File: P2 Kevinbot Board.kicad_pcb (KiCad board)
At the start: 2 copper layers, 196.5 x 95.4 mm, 76 parts, among them J1 Screw_Terminal_01x02, J10 Conn_01x04, J11 Conn_01x04_Male, J12 Conn_02x06_Odd_Even, J13 Conn_01x04, J14 Conn_01x02, J15 Conn_01x04, J16 Conn_02x06_Odd_Even, J17 Conn_04x03_Servo, J18 Conn_04x03_Servo, J19 Conn_04x03_Servo, J2 Conn_01x03_Male, J20 Conn_04x03_Servo, J21 Conn_01x02, J22 Conn_01x05, J23 Conn_01x05, J24 Conn_01x05, J25 Conn_01x05, J26 Conn_04x03_Servo, J27 Conn_04x03_Servo, J28 Conn_04x03_Servo, J29 Conn_04x03_Servo, J3 Screw_Terminal_01x02, J30 Conn_01x02_Pin, J31 Conn_01x02, J4 Screw_Terminal_01x02, J5 Screw_Terminal_01x02, J6 Conn_02x06_Odd_Even, J7 Conn_01x04, J8 Conn_02x06_Odd_Even, J9 Screw_Terminal_01x02, Q1 IRLML6402, SW1 SW_Push, U1 P2_EDGE_MODULE_SOCKET, U2 DS18B20, U3 PCA9685PW, U4 TC4427, U5 PCA9685PW

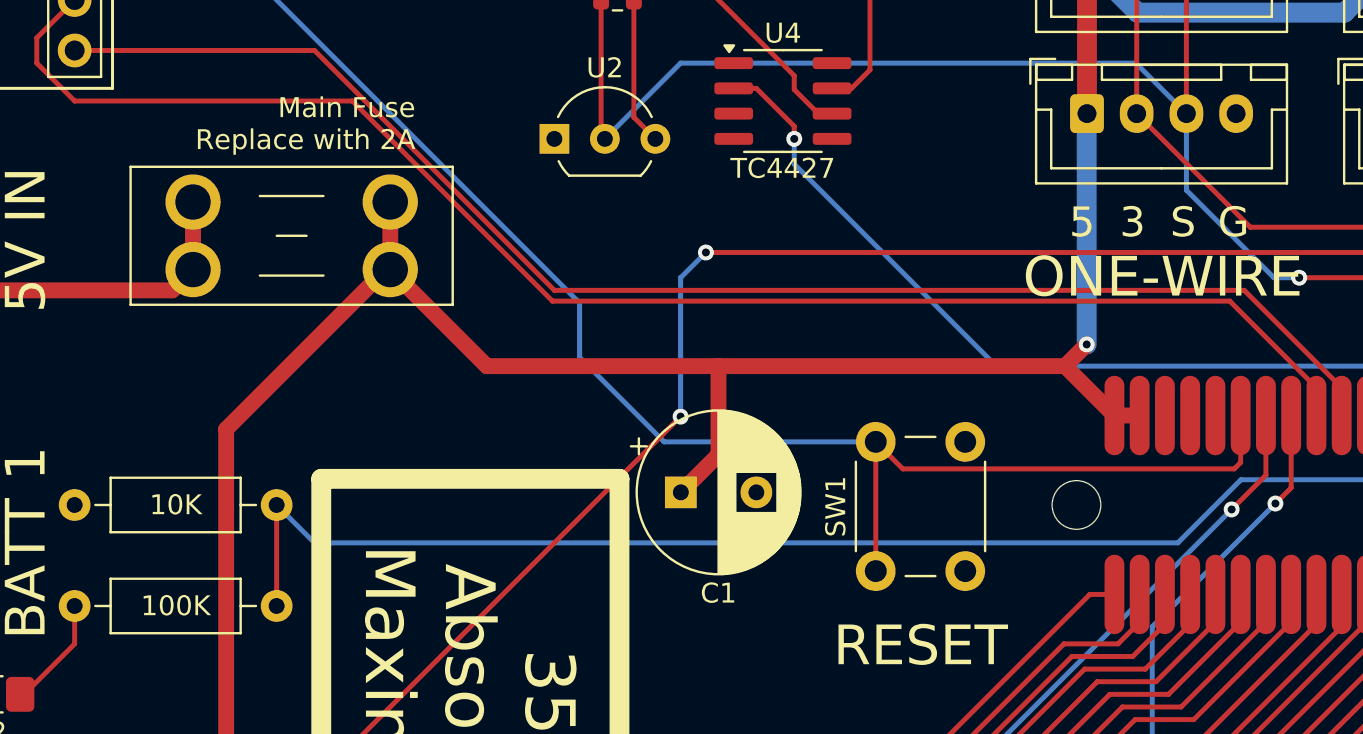
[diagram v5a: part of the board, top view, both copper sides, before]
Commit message: Add mfr part numbers and datasheets to all
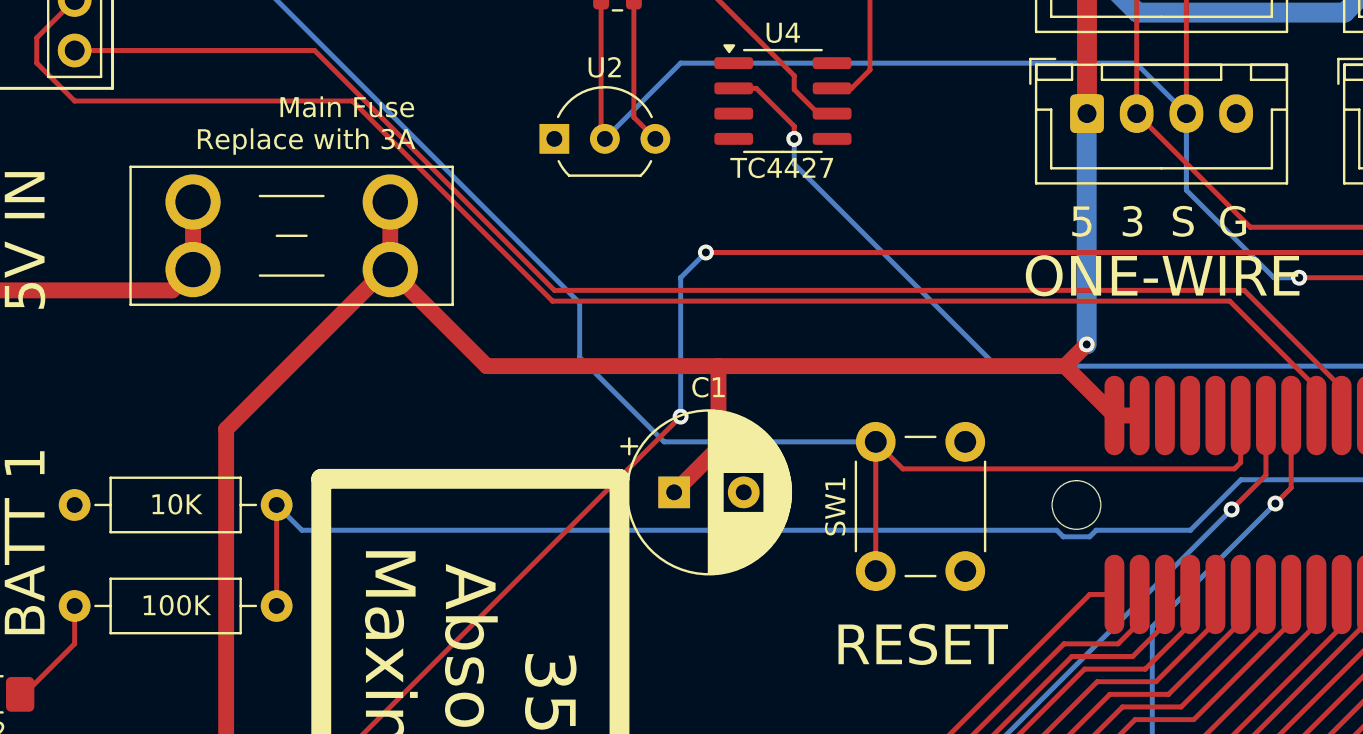
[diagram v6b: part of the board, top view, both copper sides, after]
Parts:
- C1: footprint Capacitor_THT:CP_Radial_D8.0mm_P3.80mm -> Capacitor_THT:CP_Radial_D8.0mm_P3.50mm
- moved C1 0.33 mm to (117.3, 102.2)
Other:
- board text added: "Main Fuse Replace with 3A"
- board text removed: "Main Fuse Replace with 2A"

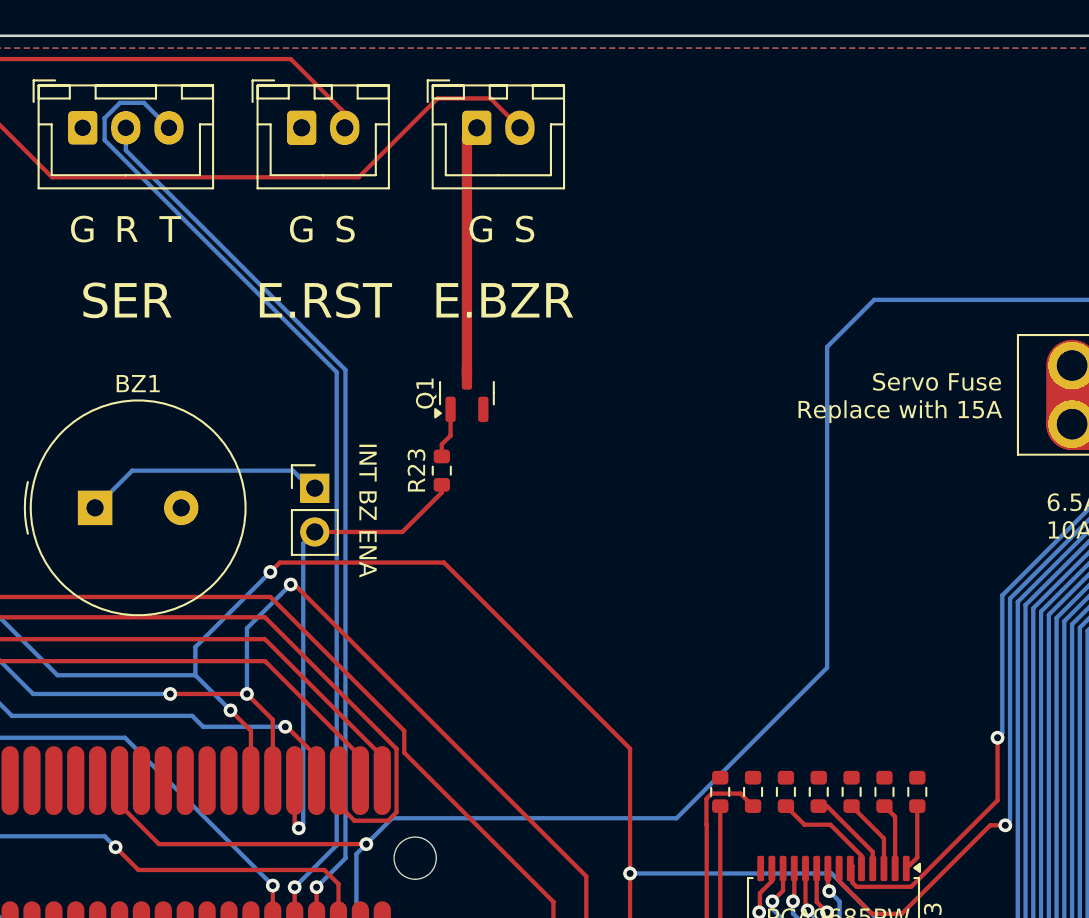
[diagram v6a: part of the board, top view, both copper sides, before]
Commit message: Add rx/tx leds, schematic cleanup
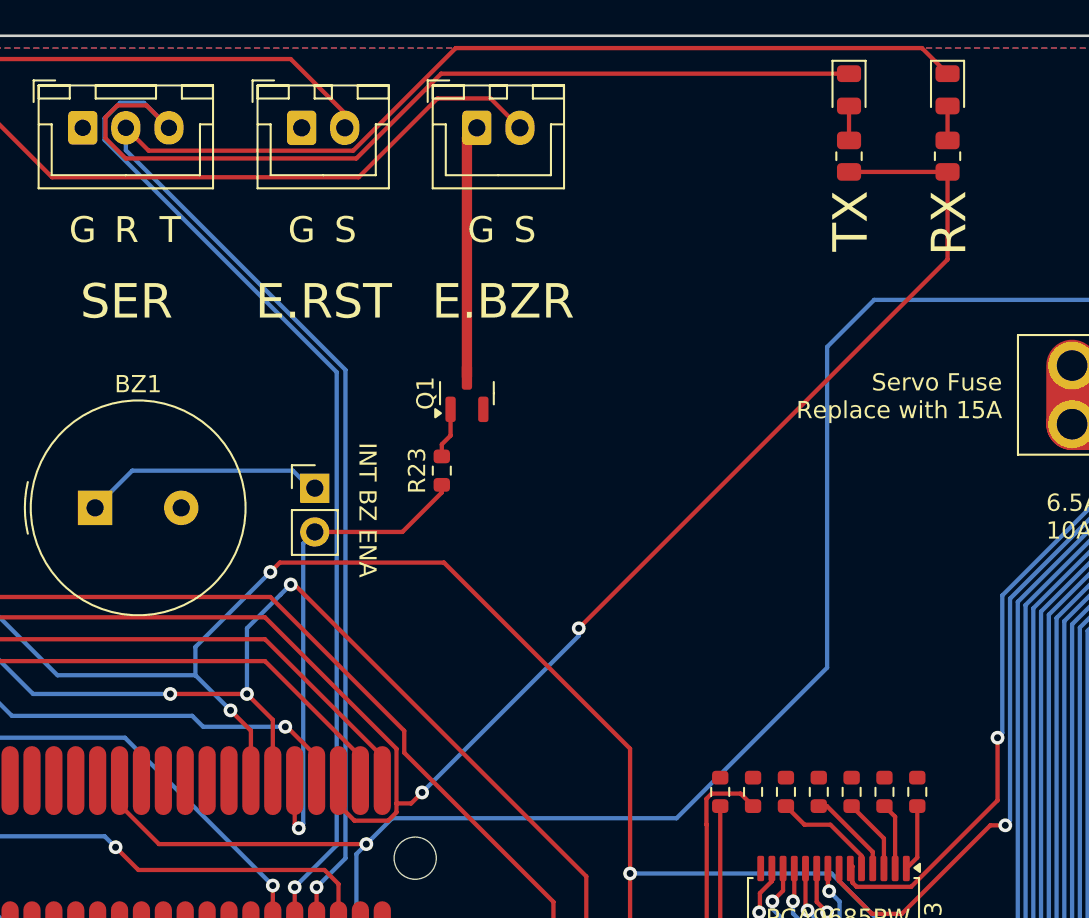
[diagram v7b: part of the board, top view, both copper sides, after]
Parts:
- added D4: LED, LED_SMD:LED_0805_2012Metric, F.Cu at (221.8, 58.3)
- added D5: LED, LED_SMD:LED_0805_2012Metric, F.Cu at (216.0, 58.3)
- added R24: 140R, Resistor_SMD:R_0805_2012Metric, F.Cu at (221.8, 62.2)
- added R25: 140R, Resistor_SMD:R_0805_2012Metric, F.Cu at (216.0, 62.2)
- R1: value 620R -> 330R
- R2: value 270R -> 140R
- R3: value 820R -> 430R
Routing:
- net P2_V32: track 122.4 -> 178.5 mm, vias 1 -> 3
- net P2_P35: track 58.7 -> 110.1 mm
- net P2_P36: track 52.8 -> 104.1 mm
- net Net-(D5-A): track 0.00 -> 2.00 mm
- net Net-(D4-A): track 0.00 -> 2.00 mm
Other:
- board text added: "RX"
- board text added: "TX"

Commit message: Add rsl
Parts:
- added J32: Conn_01x02, Connector_JST:JST_XH_B2B-XH-A_1x02_P2.50mm_Vertical, F.Cu at (127.8, 60.5)
- added Q2: IRLML6402, Package_TO_SOT_SMD:SOT-23, F.Cu at (132.5, 73.4)
- added R26: 680R, Resistor_SMD:R_0603_1608Metric, F.Cu at (131.6, 77.3)
- moved J21 7.00 mm to (117.6, 60.5)
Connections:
- J21 pad 1: GND -> BODY_LED
- J21 pad 2: BODY_LED -> GND
- U1 pad 56: unconnected-(U1-P56/LED-Pad56) -> P2_P56
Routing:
- net P2_P56: track 0.00 -> 37.3 mm, vias 0 -> 2
- net LED_PWR: track 29.3 -> 57.8 mm
- net Net-(J32-Pin_2): track 0.00 -> 13.5 mm
- net BODY_LED: track 22.8 -> 26.7 mm
- net Net-(Q2-G): track 0.00 -> 2.16 mm
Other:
- board text added: "33v Absolute Maximum"
- board text added: "RSL OUT"
- board text removed: "35v Absolute Maximum"
